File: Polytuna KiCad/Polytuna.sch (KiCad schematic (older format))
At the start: 24 parts

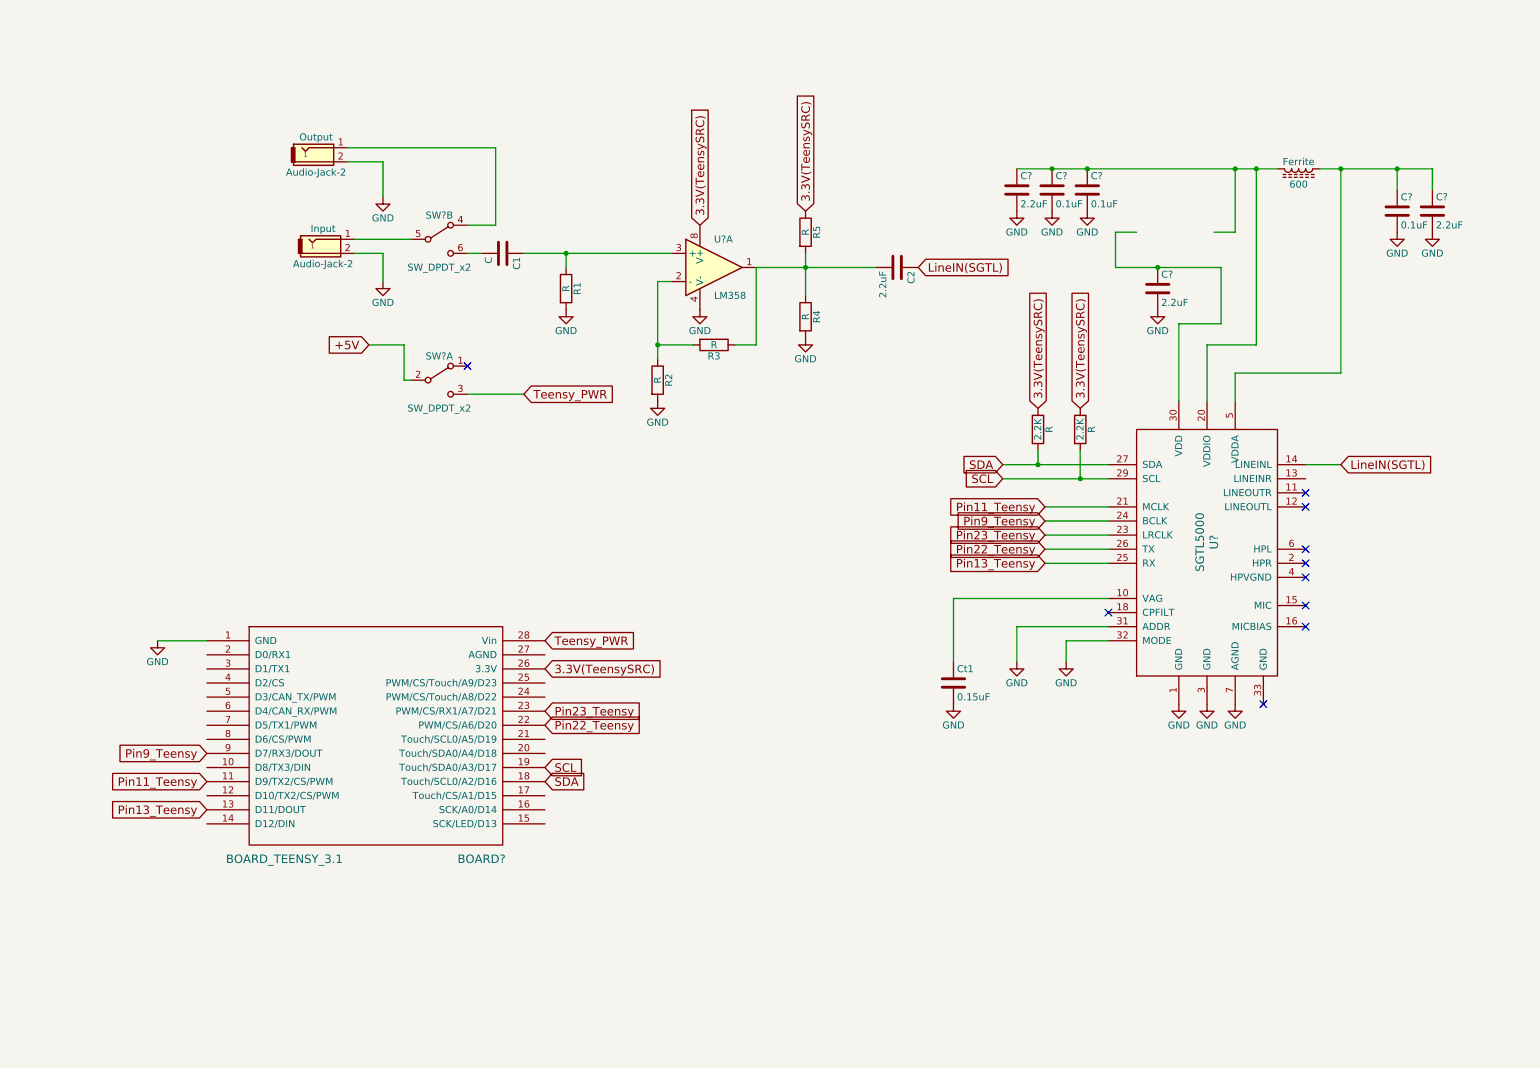
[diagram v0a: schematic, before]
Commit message: Added some switches, LEDs and jumpers
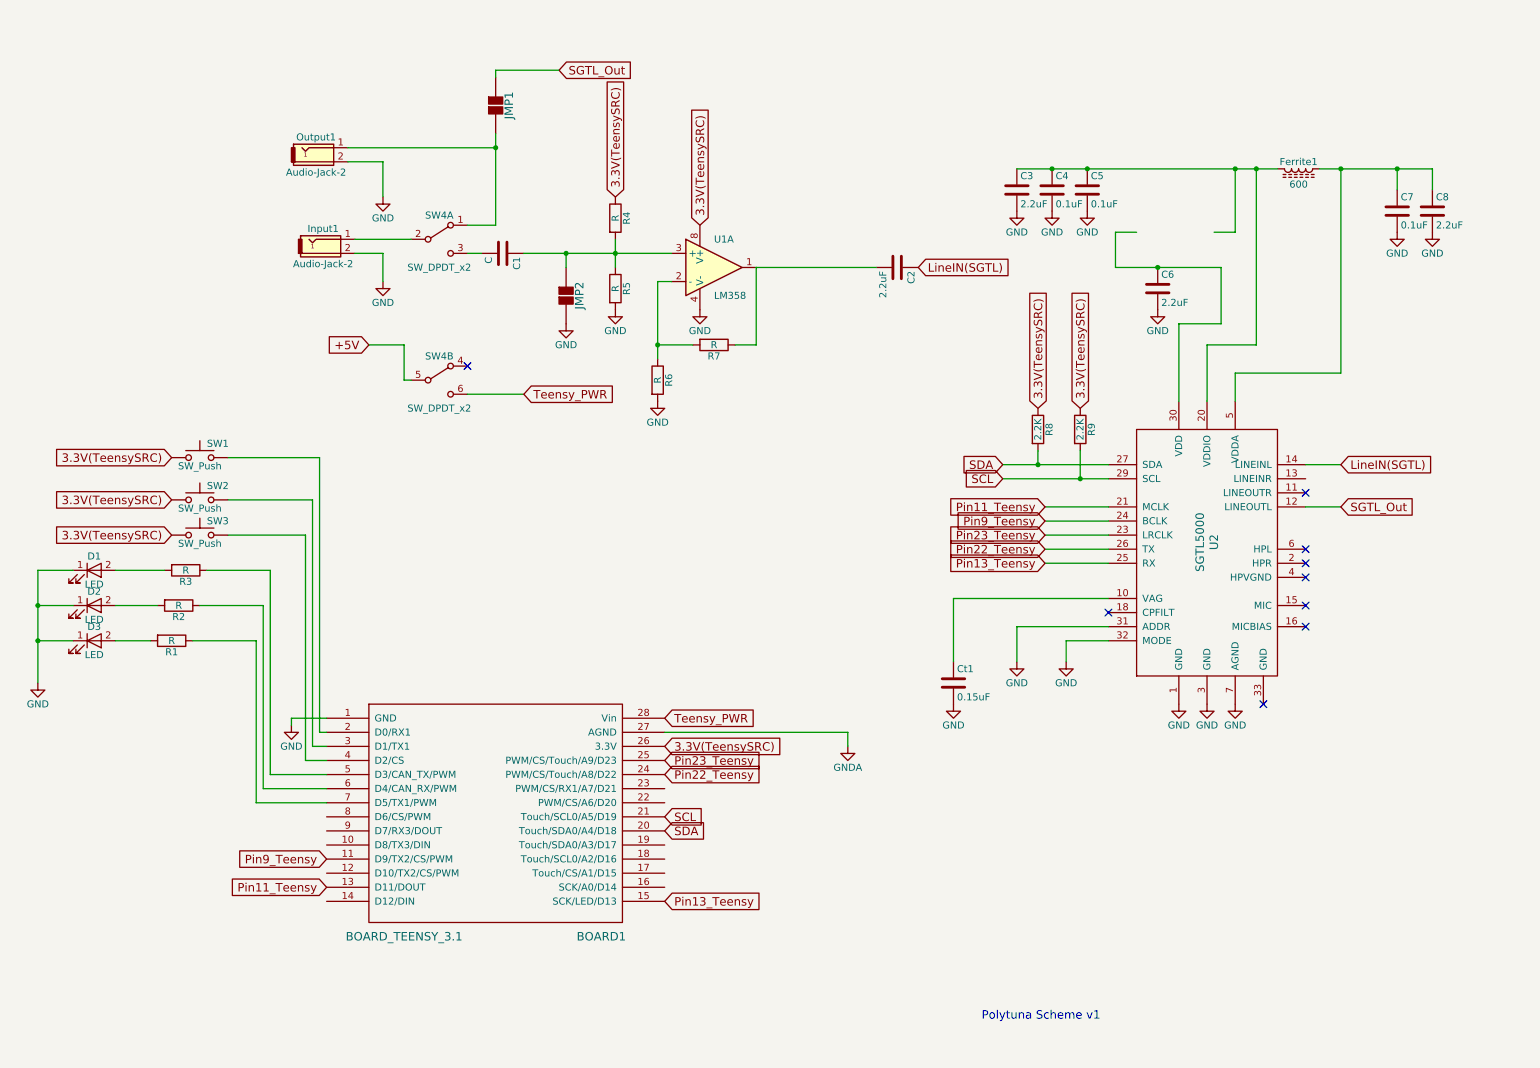
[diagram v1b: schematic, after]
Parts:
- added D1, D2, D3: LED, symbol LED
- added JMP1, JMP2: 2Jumper, symbol 2Jumper
- added R2, R3: R, symbol R
- added SW1, SW2, SW3: SW_Push, symbol SW_Push
- gave numbers to parts that had none: 10
- renumbered Ferrite to Ferrite1, Input to Input1, Output to Output1, R5 to R4, R4 to R5, R2 to R6, R3 to R7, R to R8, R to R9
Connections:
- net labels added: GNDA, SGTL_Out
- wire segments 57 -> 88
- no-connect marks 10 -> 9
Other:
- note added: "Polytuna Scheme v1\n"
- moved on the sheet: BOARD1, R4, R5

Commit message: Add switches, LEDs and jumpers
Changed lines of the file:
@@
 LIBS:kicad-library
 LIBS:teensy_3_2_full
+LIBS:pot_with_shield
+LIBS:switch_dpdt
+LIBS:ws2812b
 LIBS:Polytuna-cache
 EELAYER 25 0
@@
 Text GLabel 5100 6650 2    60   Input ~ 0
 Pin13_Teensy
-Text GLabel 5100 6150 2    60   Input ~ 0
+Text GLabel 6150 6150 2    60   Input ~ 0
 SDA
-Text GLabel 5100 6050 2    60   Input ~ 0
+Text GLabel 6150 6050 2    60   Input ~ 0
 SCL
 Text GLabel 5100 5350 2    60   Input ~ 0
@@
 	1    0    0    -1
 $EndComp
-Wire Wire Line
-	4100 2050 5150 2050
-Wire Wire Line
-	4400 2050 4400 2150
-Connection ~ 4400 2050
-Wire Wire Line
-	5050 2250 5050 2800
-Wire Wire Line
-	5050 2700 5300 2700
-Wire Wire Line
-	5750 2150 5750 2700
-Wire Wire Line
-	5750 2700 5600 2700
-Wire Wire Line
-	5050 2250 5150 2250
-Connection ~ 5050 2700
-Wire Wire Line
-	3100 2050 3100 2250
-Wire Wire Line
-	3000 2700 3250 2700
-Wire Wire Line
-	3250 2700 3250 2950
-Wire Wire Line
-	3250 2950 3300 2950
-Wire Wire Line
-	2900 1950 3300 1950
-Wire Wire Line
-	2900 2050 3100 2050
-Wire Wire Line
-	3700 2050 3800 2050
-Wire Wire Line
-	3900 1850 3700 1850
-Wire Wire Line
-	3900 1200 3900 1850
-Wire Wire Line
-	3900 1300 2850 1300
-Wire Wire Line
-	2850 1400 3100 1400
-Wire Wire Line
-	3100 1400 3100 1650
-Wire Wire Line
-	4100 3050 3700 3050
-Wire Wire Line
-	7150 4500 8250 4500
-Wire Wire Line
-	7150 4500 7150 4950
-Wire Wire Line
-	8250 4700 7600 4700
-Wire Wire Line
-	7600 4700 7600 4950
-Wire Wire Line
-	8250 4800 7950 4800
-Wire Wire Line
-	7950 4800 7950 4950
-Wire Wire Line
-	7500 3550 8250 3550
-Wire Wire Line
-	7750 3450 7750 3550
-Connection ~ 7750 3550
-Wire Wire Line
-	7500 3650 8250 3650
-Wire Wire Line
-	8050 3450 8050 3650
-Connection ~ 8050 3650
-Wire Wire Line
-	8250 3850 7800 3850
-Wire Wire Line
-	7800 3950 8250 3950
-Wire Wire Line
-	8250 4050 7800 4050
-Wire Wire Line
-	7800 4150 8250 4150
-Wire Wire Line
-	8250 4250 7800 4250
-Wire Wire Line
-	9900 3550 9650 3550
-Wire Wire Line
-	9150 3100 9150 2900
-Wire Wire Line
-	9150 2900 9900 2900
-Wire Wire Line
-	9900 2900 9900 1450
-Wire Wire Line
-	8950 3100 8950 2700
-Wire Wire Line
-	8950 2700 9300 2700
-Wire Wire Line
-	9300 2700 9300 1450
-Wire Wire Line
-	7600 1450 9450 1450
-Wire Wire Line
-	8750 3100 8750 2550
-Wire Wire Line
-	8750 2550 9050 2550
-Wire Wire Line
-	9050 2550 9050 2150
-Wire Wire Line
-	9050 2150 8300 2150
-Connection ~ 9300 1450
-Wire Wire Line
-	9750 1450 10550 1450
-Connection ~ 9900 1450
-Wire Wire Line
-	10550 1450 10550 1600
-Wire Wire Line
-	10300 1450 10300 1600
-Connection ~ 10300 1450
-Connection ~ 8100 1450
-Connection ~ 7850 1450
-Wire Wire Line
-	8300 2150 8300 1900
-Wire Wire Line
-	8300 1900 8450 1900
-Connection ~ 8600 2150
-Wire Wire Line
-	9150 1450 9150 1900
-Wire Wire Line
-	9150 1900 9000 1900
-Connection ~ 9150 1450
-Wire Wire Line
-	9900 3850 9650 3850
-Wire Wire Line
-	4750 1950 4750 2150
-Connection ~ 4750 2050
-Wire Wire Line
-	6600 2150 5750 2150
-Wire Wire Line
-	4350 750  3900 750
-Wire Wire Line
-	3900 750  3900 800
-Connection ~ 3900 1300
-Wire Wire Line
-	2700 5450 2650 5450
-Wire Wire Line
-	2650 5450 2650 3500
-Wire Wire Line
-	2650 3500 2000 3500
-Wire Wire Line
-	2700 5550 2600 5550
-Wire Wire Line
-	2600 5550 2600 3800
-Wire Wire Line
-	2600 3800 2000 3800
-Wire Wire Line
-	2700 5650 2550 5650
-Wire Wire Line
-	2550 5650 2550 4050
-Wire Wire Line
-	2550 4050 2000 4050
-Wire Wire Line
-	2700 5750 2300 5750
-Wire Wire Line
-	2300 5750 2300 4300
-Wire Wire Line
-	1550 4300 1200 4300
-Wire Wire Line
-	2700 5850 2250 5850
-Wire Wire Line
-	2250 5850 2250 4550
-Wire Wire Line
-	1500 4550 1200 4550
-Wire Wire Line
-	2700 5950 2200 5950
-Wire Wire Line
-	2200 5950 2200 4800
-Wire Wire Line
-	1450 4800 1200 4800
-Wire Wire Line
-	2700 5350 2450 5350
-Wire Wire Line
-	2450 5350 2450 5400
-Wire Wire Line
-	5100 5450 6400 5450
-Wire Wire Line
-	6400 5450 6400 5550
-Wire Wire Line
-	900  4800 650  4800
-Wire Wire Line
-	650  4300 650  5100
-Wire Wire Line
-	900  4550 650  4550
-Connection ~ 650  4800
-Wire Wire Line
-	900  4300 650  4300
-Connection ~ 650  4550
 Text GLabel 1600 3800 0    60   Input ~ 0
 3.3V(TeensySRC)
@@
 $EndComp
 Wire Wire Line
+	4100 2050 5150 2050
+Wire Wire Line
+	4400 2050 4400 2150
+Connection ~ 4400 2050
+Wire Wire Line
+	5050 2250 5050 2800
+Wire Wire Line
+	5050 2700 5300 2700
+Wire Wire Line
+	5750 2150 5750 2700
+Wire Wire Line
+	5750 2700 5600 2700
+Wire Wire Line
+	5050 2250 5150 2250
+Connection ~ 5050 2700
+Wire Wire Line
+	3100 2050 3100 2250
+Wire Wire Line
+	3000 2700 3250 2700
+Wire Wire Line
+	3250 2700 3250 2950
+Wire Wire Line
+	3250 2950 3300 2950
+Wire Wire Line
+	2900 1950 3300 1950
+Wire Wire Line
+	2900 2050 3100 2050
+Wire Wire Line
+	3700 2050 3800 2050
+Wire Wire Line
+	3900 1850 3700 1850
+Wire Wire Line
+	3900 1200 3900 1850
+Wire Wire Line
+	3900 1300 2850 1300
+Wire Wire Line
+	2850 1400 3100 1400
+Wire Wire Line
+	3100 1400 3100 1650
+Wire Wire Line
+	4100 3050 3700 3050
+Wire Wire Line
+	7150 4500 8250 4500
+Wire Wire Line
+	7150 4500 7150 4950
+Wire Wire Line
+	8250 4700 7600 4700
+Wire Wire Line
+	7600 4700 7600 4950
+Wire Wire Line
+	8250 4800 7950 4800
+Wire Wire Line
+	7950 4800 7950 4950
+Wire Wire Line
+	7500 3550 8250 3550
+Wire Wire Line
+	7750 3450 7750 3550
+Connection ~ 7750 3550
+Wire Wire Line
+	7500 3650 8250 3650
+Wire Wire Line
+	8050 3450 8050 3650
+Connection ~ 8050 3650
+Wire Wire Line
+	8250 3850 7800 3850
+Wire Wire Line
+	7800 3950 8250 3950
+Wire Wire Line
+	8250 4050 7800 4050
+Wire Wire Line
+	7800 4150 8250 4150
+Wire Wire Line
+	8250 4250 7800 4250
+Wire Wire Line
+	9900 3550 9650 3550
+Wire Wire Line
+	9150 3100 9150 2900
+Wire Wire Line
+	9150 2900 9900 2900
+Wire Wire Line
+	9900 2900 9900 1450
+Wire Wire Line
+	8950 3100 8950 2700
+Wire Wire Line
+	8950 2700 9300 2700
+Wire Wire Line
+	9300 2700 9300 1450
+Wire Wire Line
+	7600 1450 9450 1450
+Wire Wire Line
+	8750 3100 8750 2550
+Wire Wire Line
+	8750 2550 9050 2550
+Wire Wire Line
+	9050 2550 9050 2150
+Wire Wire Line
+	9050 2150 8300 2150
+Connection ~ 9300 1450
+Wire Wire Line
+	9750 1450 10550 1450
+Connection ~ 9900 1450
+Wire Wire Line
+	10550 1450 10550 1600
+Wire Wire Line
+	10300 1450 10300 1600
+Connection ~ 10300 1450
+Connection ~ 8100 1450
+Connection ~ 7850 1450
+Wire Wire Line
+	8300 2150 8300 1900
+Wire Wire Line
+	8300 1900 8450 1900
+Connection ~ 8600 2150
+Wire Wire Line
+	9150 1450 9150 1900
+Wire Wire Line
+	9150 1900 9000 1900
+Connection ~ 9150 1450
+Wire Wire Line
+	9900 3850 9650 3850
+Wire Wire Line
+	4750 1950 4750 2150
+Connection ~ 4750 2050
+Wire Wire Line
+	6600 2150 5750 2150
+Wire Wire Line
+	4350 750  3900 750
+Wire Wire Line
+	3900 750  3900 800
+Connection ~ 3900 1300
+Wire Wire Line
+	2700 5450 2650 5450
+Wire Wire Line
+	2650 5450 2650 3500
+Wire Wire Line
+	2650 3500 2000 3500
+Wire Wire Line
+	2700 5550 2600 5550
+Wire Wire Line
+	2600 5550 2600 3800
+Wire Wire Line
+	2600 3800 2000 3800
+Wire Wire Line
+	2700 5650 2550 5650
+Wire Wire Line
+	2550 5650 2550 4050
+Wire Wire Line
+	2550 4050 2000 4050
+Wire Wire Line
+	2700 5750 2300 5750
+Wire Wire Line
+	2300 5750 2300 4300
+Wire Wire Line
+	1550 4300 1200 4300
+Wire Wire Line
+	2700 5850 2250 5850
+Wire Wire Line
+	2250 5850 2250 4550
+Wire Wire Line
+	1500 4550 1200 4550
+Wire Wire Line
+	2700 5950 2200 5950
+Wire Wire Line
+	2200 5950 2200 4800
+Wire Wire Line
+	1450 4800 1200 4800
+Wire Wire Line
+	2700 5350 2450 5350
+Wire Wire Line
+	2450 5350 2450 5400
+Wire Wire Line
+	5100 5450 6400 5450
+Wire Wire Line
+	6400 5450 6400 5550
+Wire Wire Line
+	900  4800 650  4800
+Wire Wire Line
+	650  4300 650  5100
+Wire Wire Line
+	900  4550 650  4550
+Connection ~ 650  4800
+Wire Wire Line
+	900  4300 650  4300
+Connection ~ 650  4550
+Wire Wire Line
 	2300 4300 1850 4300
 Wire Wire Line
@@
 Wire Wire Line
 	2200 4800 1750 4800
+Wire Wire Line
+	6150 6050 5100 6050
+Wire Wire Line
+	5100 6150 6150 6150
 $EndSCHEMATC

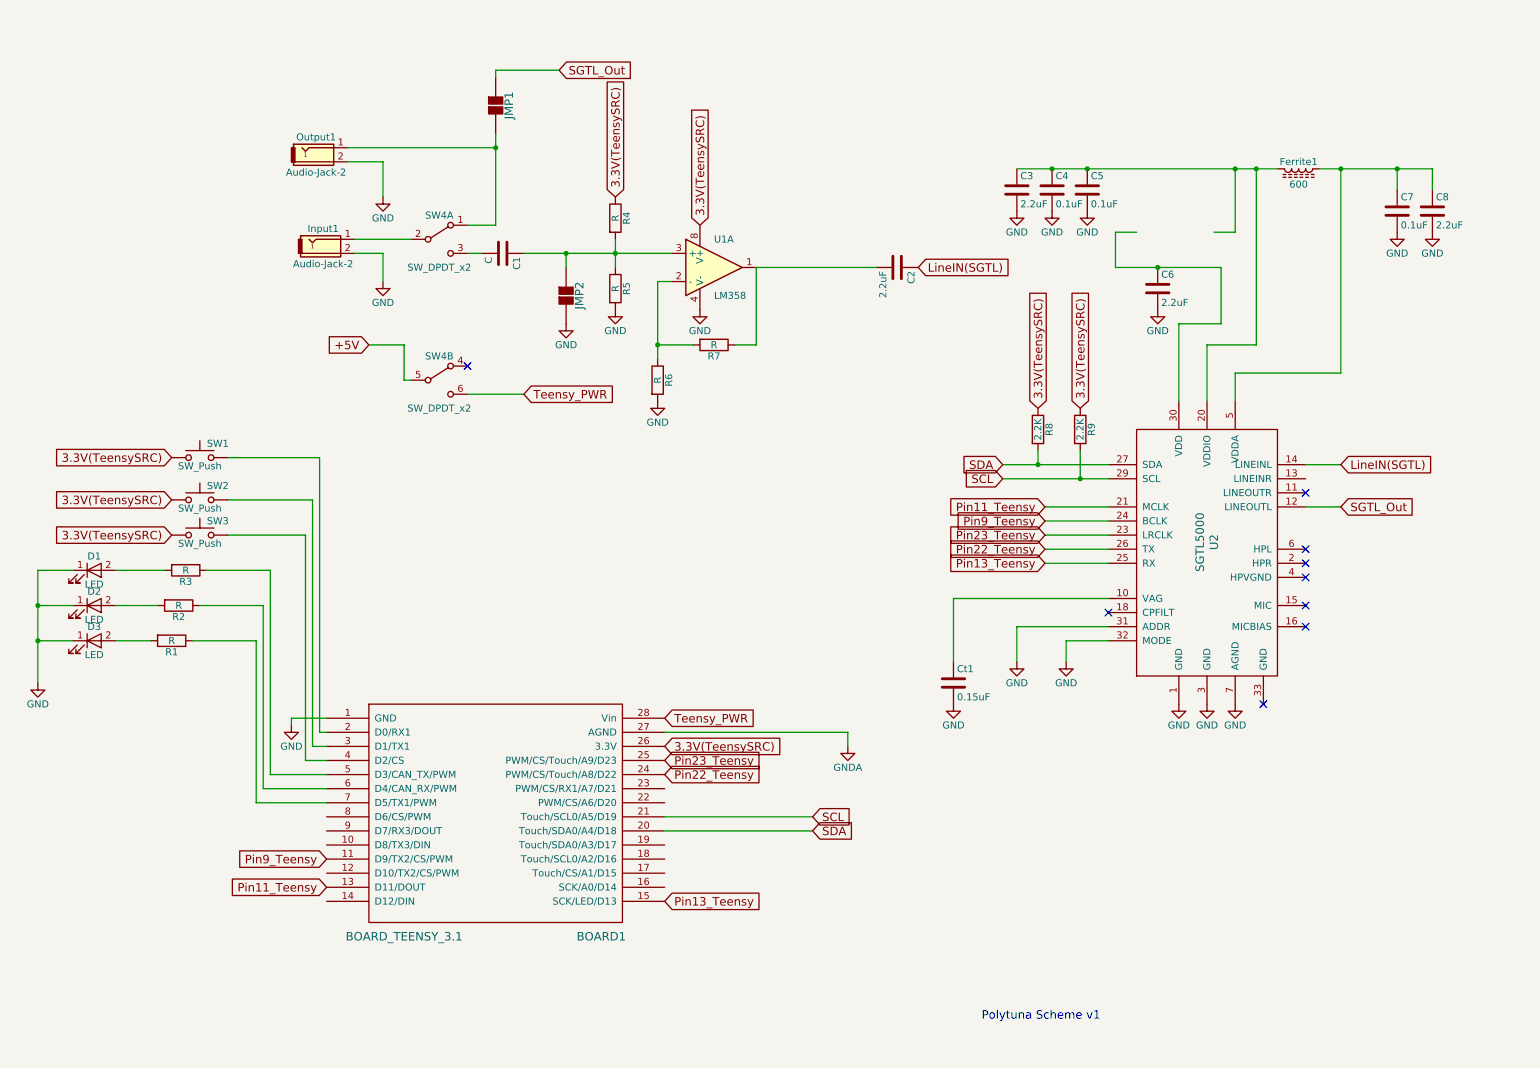
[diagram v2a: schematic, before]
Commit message: Added some pwr_flags, AP7313
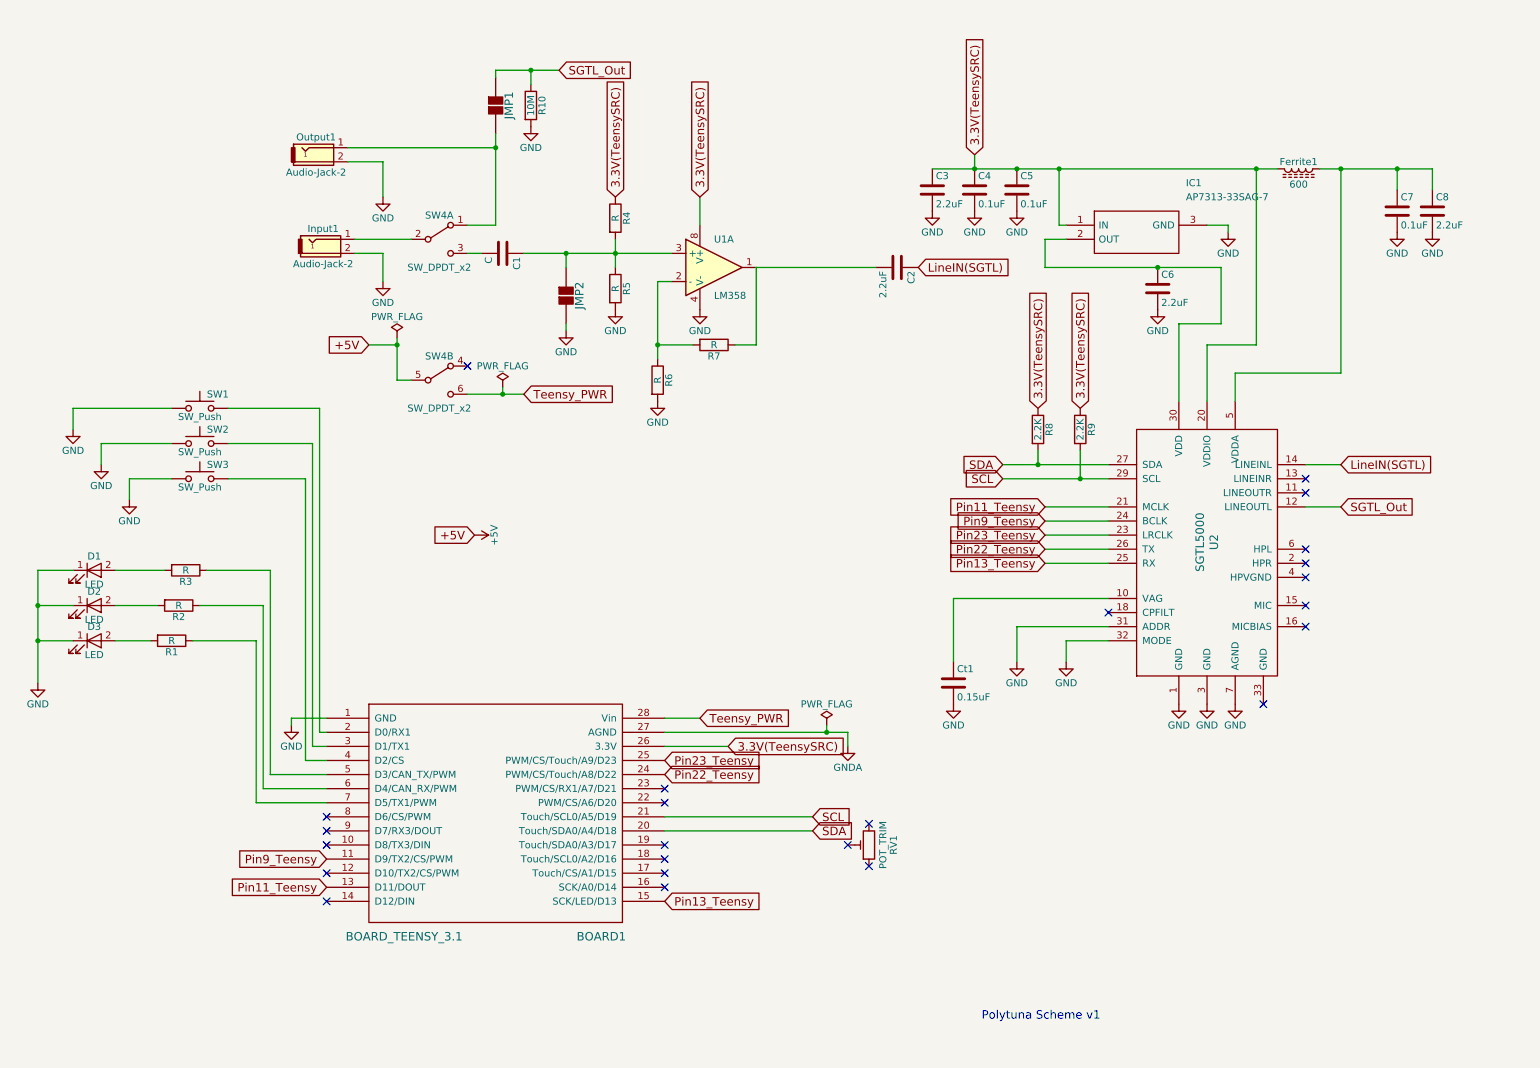
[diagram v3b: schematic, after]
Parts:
- added IC1: AP7313-33SAG-7, SOT96P240X110-3N, symbol AP7313-33SAG-7
- added R10: 10M, symbol R
- added RV1: POT_TRIM, symbol POT_TRIM
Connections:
- net 3.3V(TeensySRC): now also C3.1, C4.1, C5.1, Ferrite1.2, U2.20 (VDDIO), IC1.1 (IN); no longer SW1.1, SW2.1, SW3.1
- net GND: now also SW1.1, SW2.1, SW3.1, IC1.3 (GND), R10.2
- net SGTL_Out: now also R10.1
- net at C6.1, U2.30 (VDD): now also IC1.2 (OUT)
- no-connect marks 9 -> 24
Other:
- moved on the sheet: C3, C4, C5, SW1, SW2, SW3
